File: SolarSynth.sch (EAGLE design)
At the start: 9 parts, among them IC1 74HCT14N

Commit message: Cap changes
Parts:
- R2: value (none) -> 1k
- U$1: value 080-EU -> 2.2u
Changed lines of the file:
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@@
 <part name="BAT1" library="SparkFun-Electromechanical" deviceset="BATTERY" device="9V"/>
 <part name="R1" library="TomW" deviceset="ALPHA-9MM" device="A" technology="F2" value="STARVE"/>
-<part name="R2" library="TomW" deviceset="R-EU_" device="0207/7"/>
-<part name="U$1" library="gm-caps-electro-pol" deviceset="080-EU" device=""/>
+<part name="R2" library="TomW" deviceset="R-EU_" device="0207/7" value="1k"/>
+<part name="U$1" library="gm-caps-electro-pol" deviceset="080-EU" device="" value="2.2u"/>
 <part name="R3" library="TomW" deviceset="R-EU_" device="0207/7"/>
 <part name="R4" library="TomW" deviceset="R-EU_" device="0207/7"/>

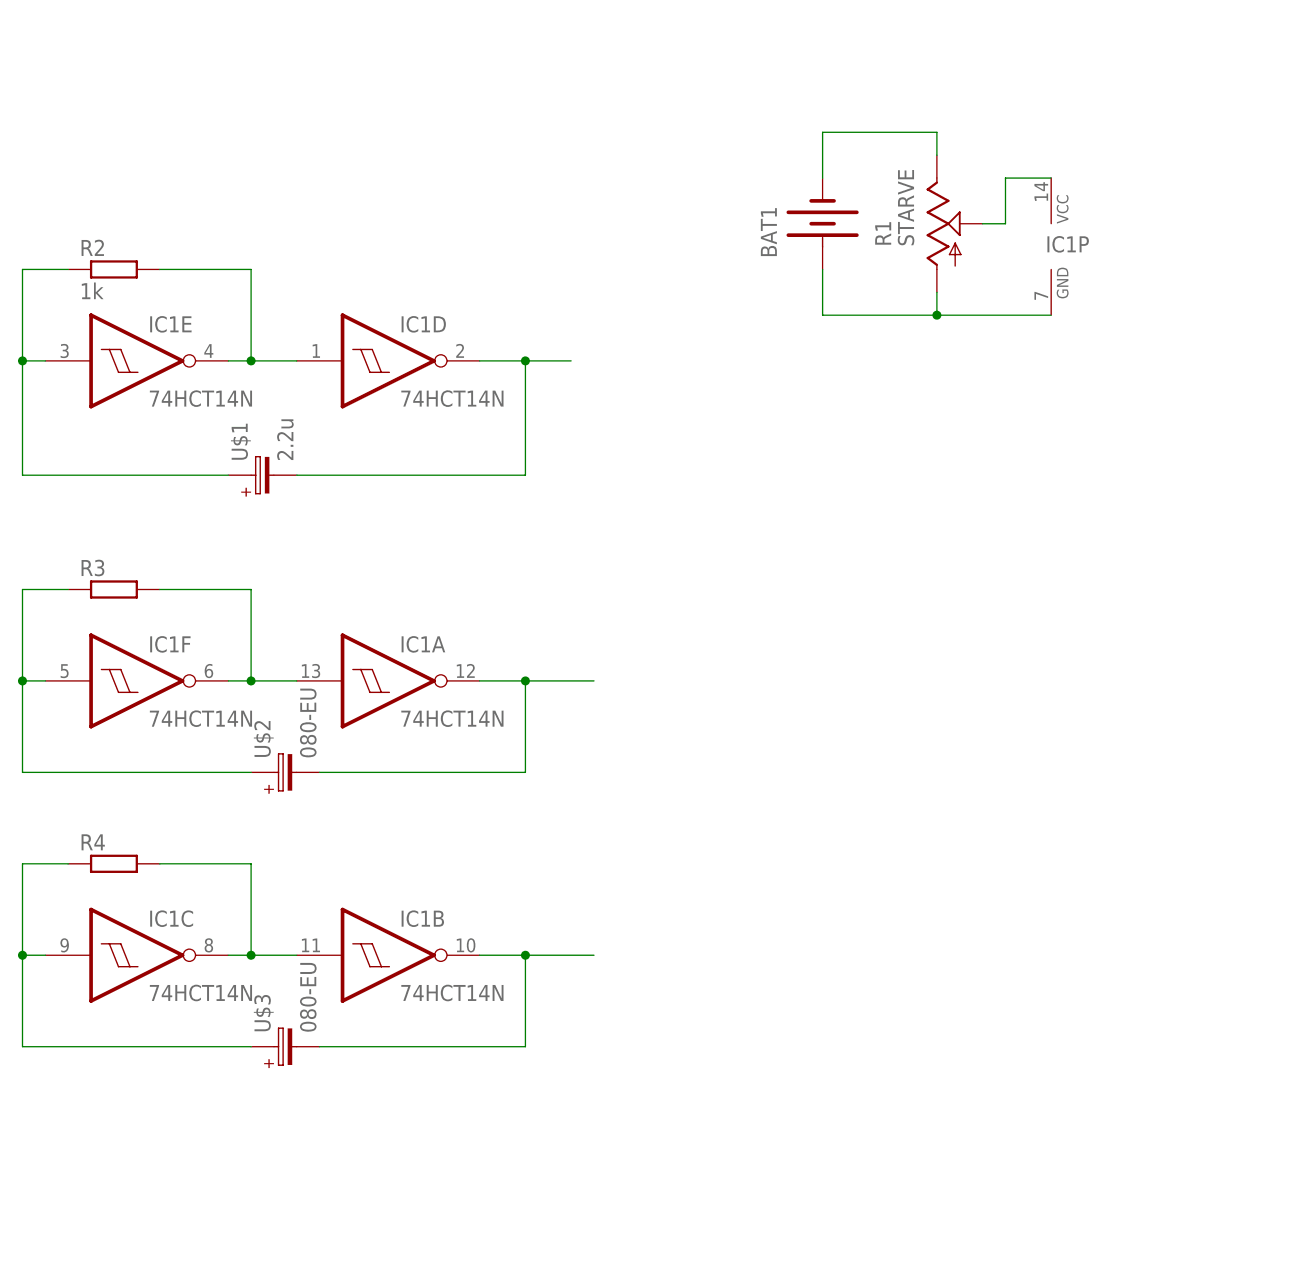
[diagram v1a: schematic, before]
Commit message: Proto gerbers to OSH park
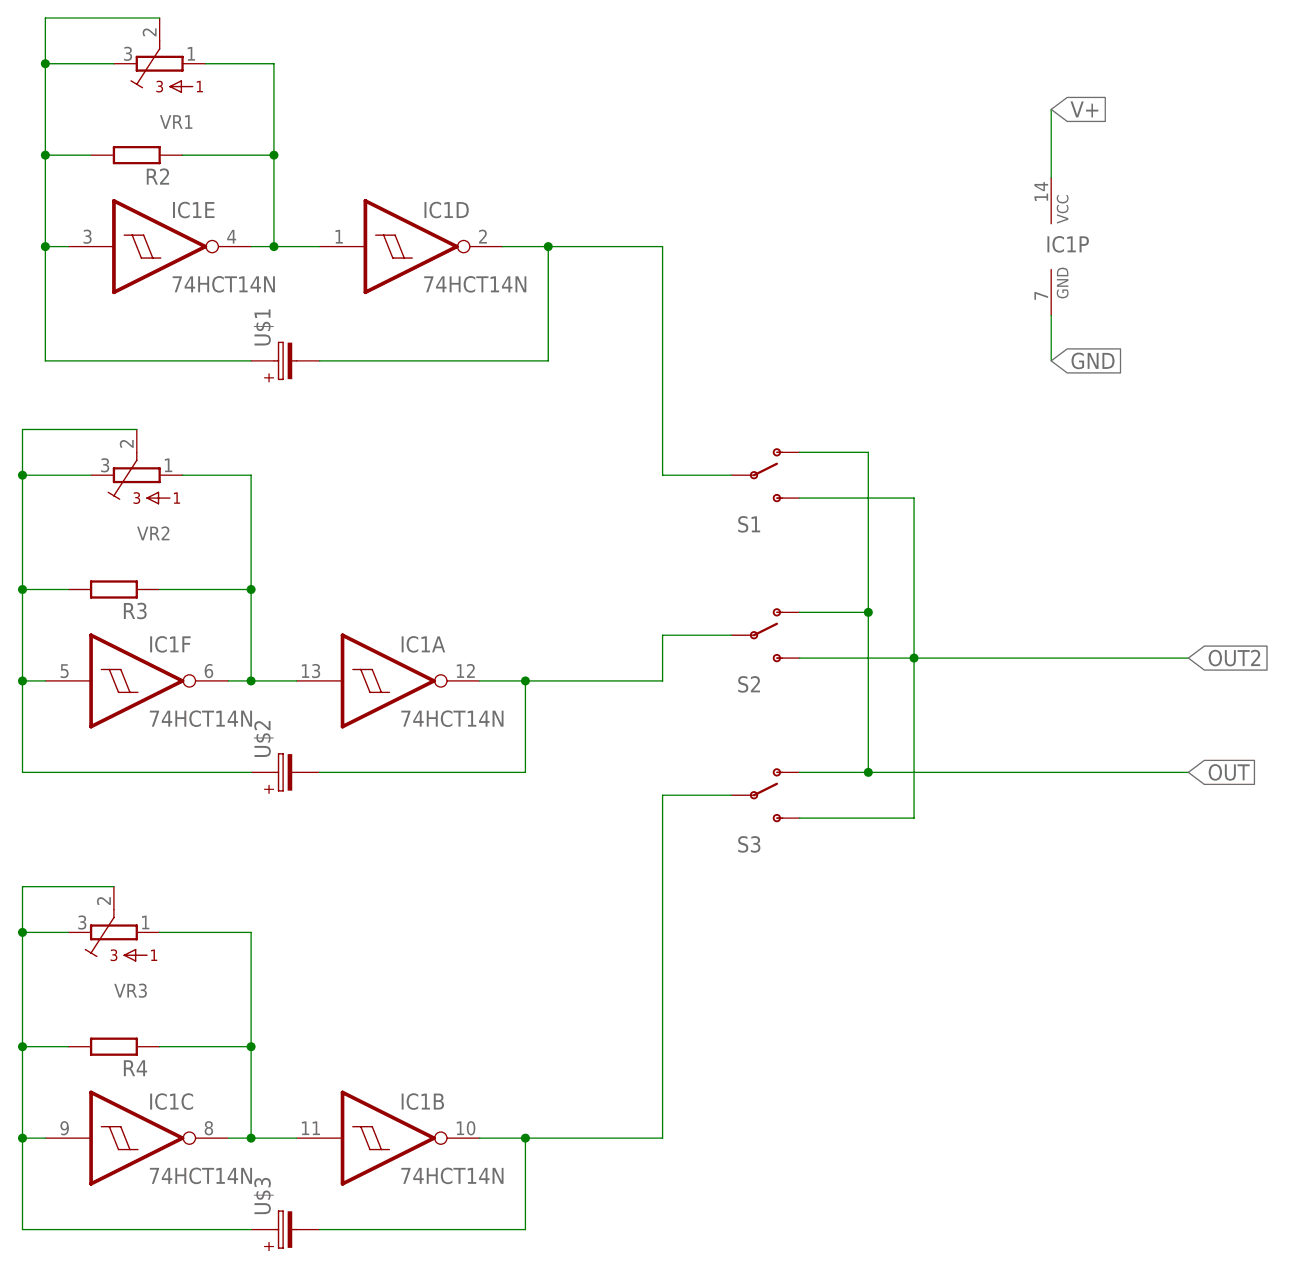
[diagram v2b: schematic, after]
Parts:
- removed BAT1: (no value), SparkFun-Electromechanical:BATTERY9V
- removed R1: STARVE, TomW:ALPHA-9MMF2A
- added S1, S2, S3: (no value), SparkFun-Electromechanical:SWITCH-SPDTKIT
- added VR1, VR2, VR3: (no value), MusicThingModular:BOURNS_3362P_TRIMMERP
- R2: value 1k -> (none)
- U$1: value 2.2u -> 080-EU
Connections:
- removed net N$1: BAT1.+, IC1P.GND, R1.A
- removed net N$2: BAT1.-, R1.E
- removed net N$3: IC1P.VCC, R1.S
- new net GND: IC1P.GND
- new net OUT: S1.O, S2.O, S3.O
- new net OUT2: S1.S, S2.S, S3.S
- new net V+: IC1P.VCC
- net N$10: now also R4.2, VR3.2, VR3.3; no longer R4.1
- net N$11: now also R4.1, VR3.1; no longer R4.2
- net N$12: now also S3.P
- net N$4: now also R2.1, VR1.1; no longer R2.2
- net N$5: now also R2.2, VR1.2, VR1.3; no longer R2.1
- net N$6: now also S1.P
- net N$7: now also R3.2, VR2.2, VR2.3; no longer R3.1
- net N$8: now also R3.1, VR2.1; no longer R3.2
- net N$9: now also S2.P
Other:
- moved on the sheet: IC1B, IC1C, IC1D, IC1E, R2, R3, R4, U$1, U$3
